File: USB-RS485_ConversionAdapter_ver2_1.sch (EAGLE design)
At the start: 26 parts, among them IC1 ADM3078E, IC2 FT232RL

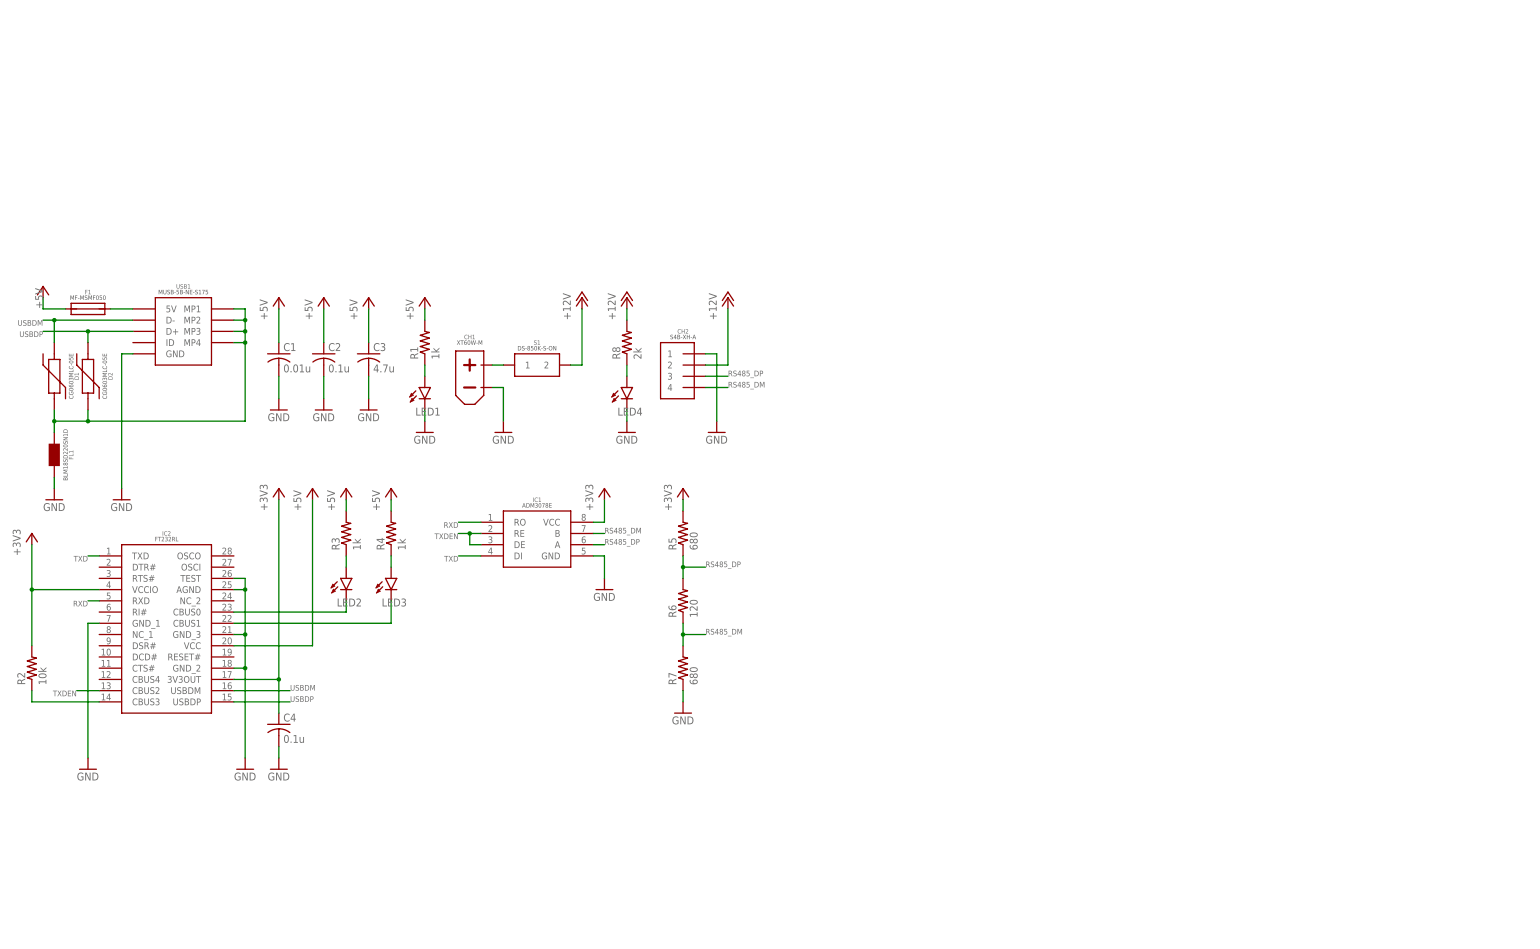
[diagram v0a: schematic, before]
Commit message: Update License and organize data
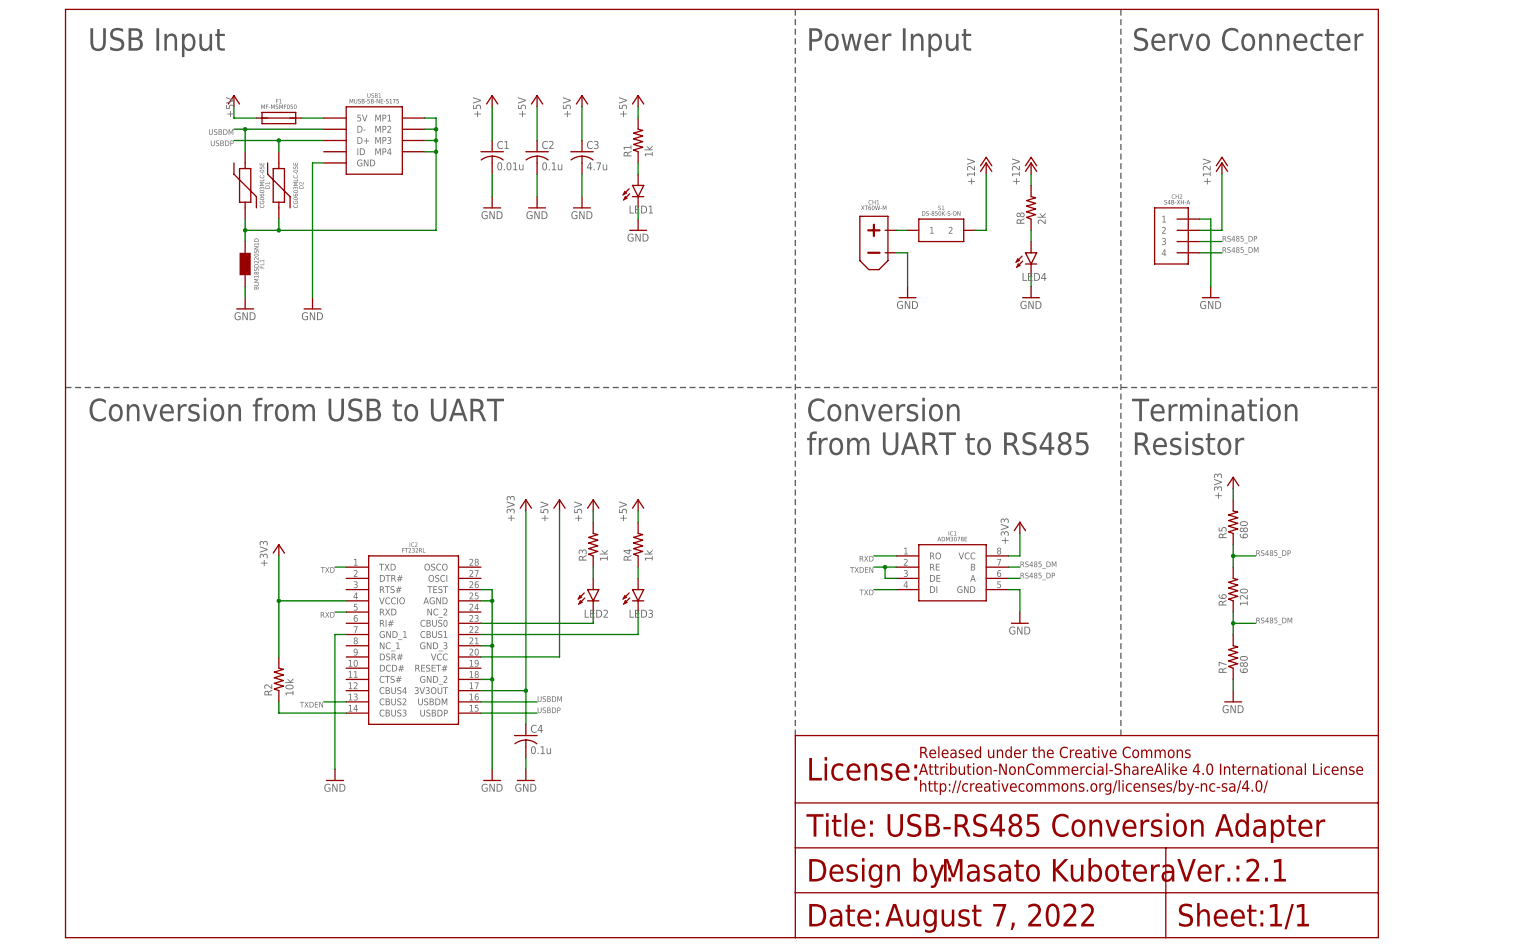
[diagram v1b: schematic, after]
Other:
- note added: "1/1"
- note added: "2.1"
- note added: "August 7, 2022"
- note added: "Conversion from UART to RS485"
- note added: "Conversion from USB to UART"
- note added: "Power Input"
- note added: "Servo Connecter"
- note added: "Termination Resistor"
- note added: "USB Input"
- note added: "USB-RS485 Conversion Adapter"
- moved on the sheet: C1, C2, C3, C4, CH1, CH2, D1, D2, F1, FL1, IC1, IC2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
